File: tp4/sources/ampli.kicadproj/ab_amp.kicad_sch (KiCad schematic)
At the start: 14 parts, among them Q201 BC327, Q202 BC327, Q203 BC337, Q204 TIP122, Q205 TIP127, U201 TL082

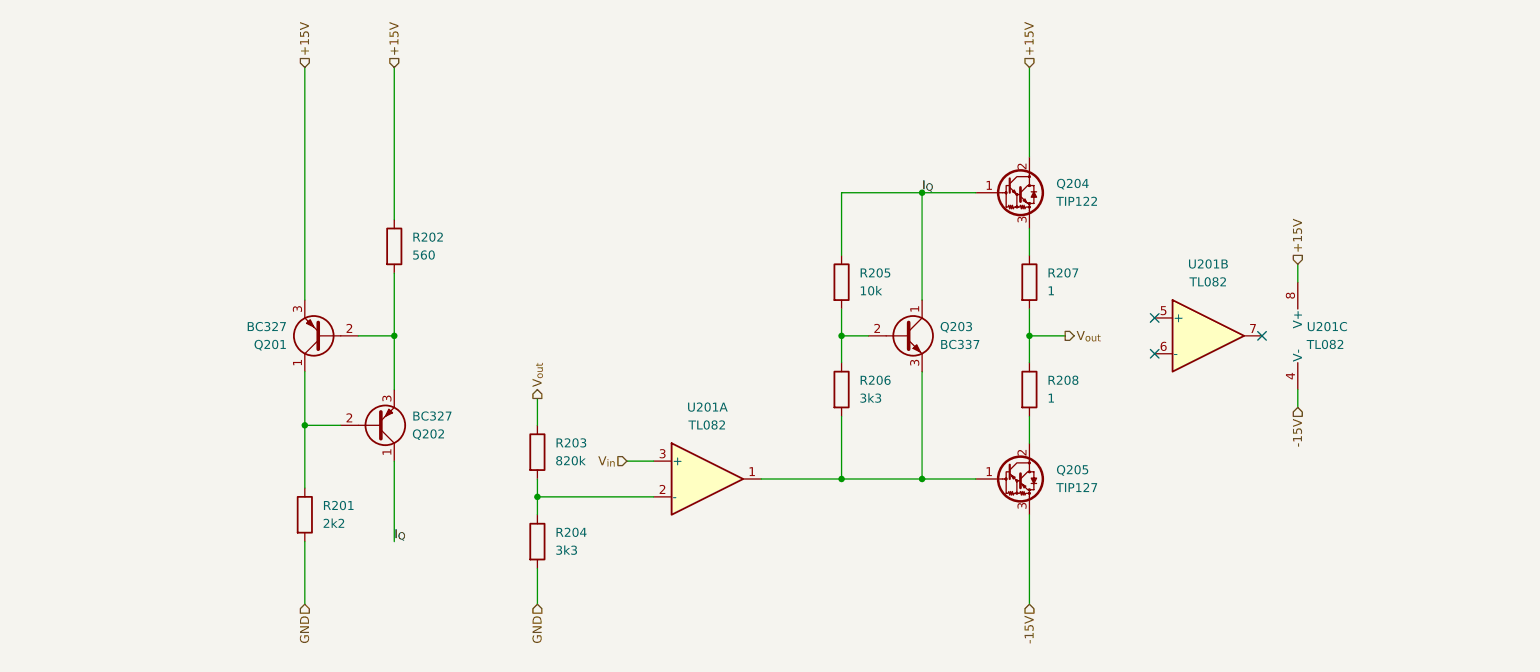
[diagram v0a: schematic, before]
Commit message: tp4: Agrega pcb y actualiza simulaciones
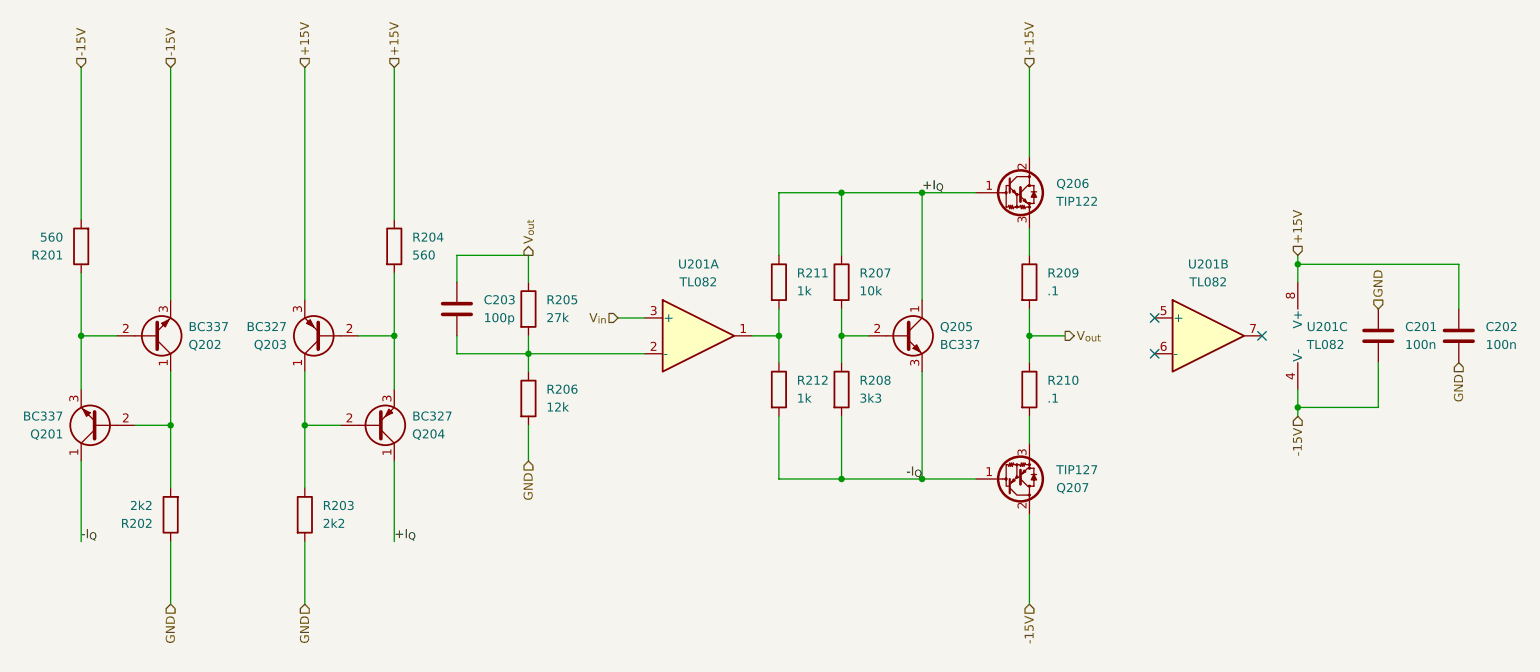
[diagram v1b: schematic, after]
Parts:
- added C201, C202: 100n, Capacitor_THT:C_Disc_D5.0mm_W2.5mm_P2.50mm, symbol Device:C
- added C203: 100p, Capacitor_THT:C_Disc_D5.0mm_W2.5mm_P2.50mm, symbol Device:C
- added Q201, Q202: BC337, Package_TO_SOT_THT:TO-92_Wide, symbol Transistor_BJT:BC337
- added R201: 560, Resistor_THT:R_Axial_DIN0207_L6.3mm_D2.5mm_P10.16mm_Horizontal, symbol Device:R
- added R202: 2k2, Resistor_THT:R_Axial_DIN0207_L6.3mm_D2.5mm_P10.16mm_Horizontal, symbol Device:R
- added R211, R212: 1k, Resistor_THT:R_Axial_DIN0207_L6.3mm_D2.5mm_P10.16mm_Horizontal, symbol Device:R
- Q203: renamed from Q201; footprint Package_TO_SOT_THT:TO-92_Inline -> Package_TO_SOT_THT:TO-92_Wide
- Q204: renamed from Q202; footprint Package_TO_SOT_THT:TO-92_Inline -> Package_TO_SOT_THT:TO-92_Wide
- Q205: renamed from Q203; footprint Package_TO_SOT_THT:TO-92_Inline -> Package_TO_SOT_THT:TO-92_Wide
- R203: renamed from R201; footprint (none) -> Resistor_THT:R_Axial_DIN0207_L6.3mm_D2.5mm_P10.16mm_Horizontal
- R204: renamed from R202; footprint (none) -> Resistor_THT:R_Axial_DIN0207_L6.3mm_D2.5mm_P10.16mm_Horizontal
- R205: renamed from R203; value 820k -> 27k; footprint (none) -> Resistor_THT:R_Axial_DIN0207_L6.3mm_D2.5mm_P10.16mm_Horizontal
- R206: renamed from R204; value 3k3 -> 12k; footprint (none) -> Resistor_THT:R_Axial_DIN0207_L6.3mm_D2.5mm_P10.16mm_Horizontal
- R207: renamed from R205; footprint (none) -> Resistor_THT:R_Axial_DIN0207_L6.3mm_D2.5mm_P10.16mm_Horizontal
- R208: renamed from R206; footprint (none) -> Resistor_THT:R_Axial_DIN0207_L6.3mm_D2.5mm_P10.16mm_Horizontal
- R209: renamed from R207; value 1 -> .1; footprint (none) -> Resistor_THT:R_Axial_DIN0516_L15.5mm_D5.0mm_P30.48mm_Horizontal
- R210: renamed from R208; value 1 -> .1; footprint (none) -> Resistor_THT:R_Axial_DIN0516_L15.5mm_D5.0mm_P30.48mm_Horizontal
- U201: footprint Package_DFN_QFN:Texas_DSQ0010A_WSON-10-1EP_2x2mm_P0.4mm_EP0.9x1.5mm -> Package_DIP:DIP-8_W7.62mm_Socket_LongPads
- renumbered Q204 to Q206, Q205 to Q207
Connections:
- net +15V: now also C202.1
- net -15V: now also Q207.2 (C), C201.2, Q202.3 (E), R201.2; no longer Q207.3 (E)
- net GND: now also C201.1, C202.2, R202.1
- net V_{out}: now also C203.1
- net -I_{Q}: now reaches Q205.3 (E), Q207.1 (B), R208.2
- net -I_{Q}: now also Q201.1 (C), R212.2; no longer U201.1
- net at R205.2, R206.1, U201.2 (-): now also C203.2
- net at R210.2: now also Q207.3 (E); no longer Q207.2 (C)
- net I_{Q} renamed +I_{Q}
- net +I_{Q}: now also R211.1
- new net: R211.2, R212.1, U201.1
- new net: Q201.3 (E), Q202.2 (B), R201.1
- new net: Q201.2 (B), Q202.1 (C), R202.2
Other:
- moved on the sheet: R205, R206, U201A
